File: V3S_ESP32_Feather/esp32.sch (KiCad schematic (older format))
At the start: 21 parts, among them J2 PWM, J4 I2C, J5 U.FL-R-SMT(01), U3 MPU-9250_Obsolete, U5 ESP32-PICO-D4, U7 BMP280

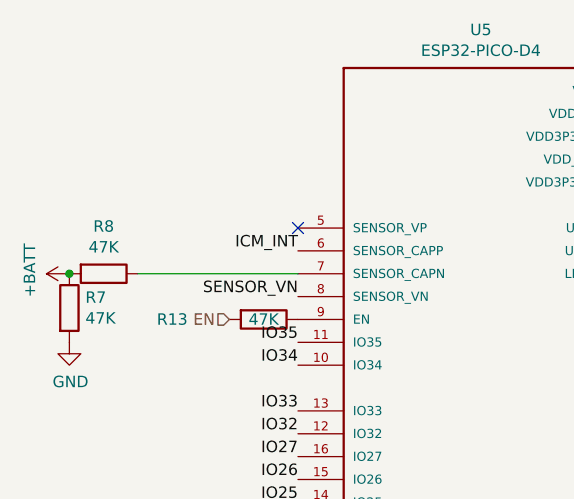
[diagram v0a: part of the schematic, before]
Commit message: fix adp322, optimize routing
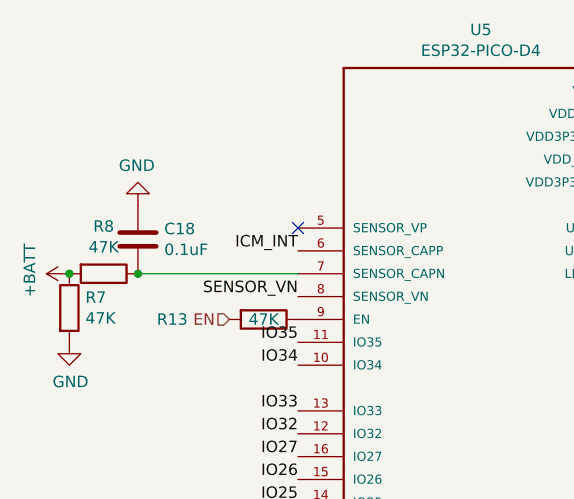
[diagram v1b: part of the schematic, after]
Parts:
- added C18: 0.1uF, Capacitor_SMD:C_0201_0603Metric, symbol Device:C
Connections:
- net GND: now also C18.2
- net at R8.1, U5.7 (SENSOR_CAPN): now also C18.1
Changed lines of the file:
@@
 Text Label 9600 3250 2    50   ~ 0
 SCL
+$Comp
+L Device:C C18
+U 1 1 5DC148DC
+P 1150 2350
+F 0 "C18" H 1035 2304 50  0000 R CNN
+F 1 "0.1uF" H 1035 2395 50  0000 R CNN
+F 2 "Capacitor_SMD:C_0201_0603Metric" H 1188 2200 50  0001 C CNN
+F 3 "~" H 1150 2350 50  0001 C CNN
+	1    1150 2350
+	-1   0    0    1
+$EndComp
+Connection ~ 1150 2500
+$Comp
+L power:GND #PWR0147
+U 1 1 5DC160B6
+P 1150 2200
+F 0 "#PWR0147" H 1150 1950 50  0001 C CNN
+F 1 "GND" H 1155 2027 50  0000 C CNN
+F 2 "" H 1150 2200 50  0001 C CNN
+F 3 "" H 1150 2200 50  0001 C CNN
+	1    1150 2200
+	-1   0    0    1
+$EndComp
 $EndSCHEMATC

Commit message: Move via from pad and rebuild fab files
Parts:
- C11: value 10nF -> 1uF
- C15, C16: value 100nF -> 0.1uF
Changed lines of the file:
@@
 P 9850 2800
 F 0 "C16" V 9598 2800 50  0000 C CNN
-F 1 "100nF" V 9689 2800 50  0000 C CNN
+F 1 "0.1uF" V 9689 2800 50  0000 C CNN
 F 2 "Capacitor_SMD:C_0201_0603Metric" H 9888 2650 50  0001 C CNN
 F 3 "~" H 9850 2800 50  0001 C CNN
@@
 P 9850 2400
 F 0 "C15" V 9598 2400 50  0000 C CNN
-F 1 "100nF" V 9689 2400 50  0000 C CNN
+F 1 "0.1uF" V 9689 2400 50  0000 C CNN
 F 2 "Capacitor_SMD:C_0201_0603Metric" H 9888 2250 50  0001 C CNN
 F 3 "~" H 9850 2400 50  0001 C CNN
@@
 P 2350 5400
 F 0 "C11" V 2100 5400 50  0000 C CNN
-F 1 "10nF" V 2200 5400 50  0000 C CNN
+F 1 "1uF" V 2200 5400 50  0000 C CNN
 F 2 "Capacitor_SMD:C_0201_0603Metric" H 2388 5250 50  0001 C CNN
 F 3 "~" H 2350 5400 50  0001 C CNN
